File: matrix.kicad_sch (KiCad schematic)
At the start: 154 parts

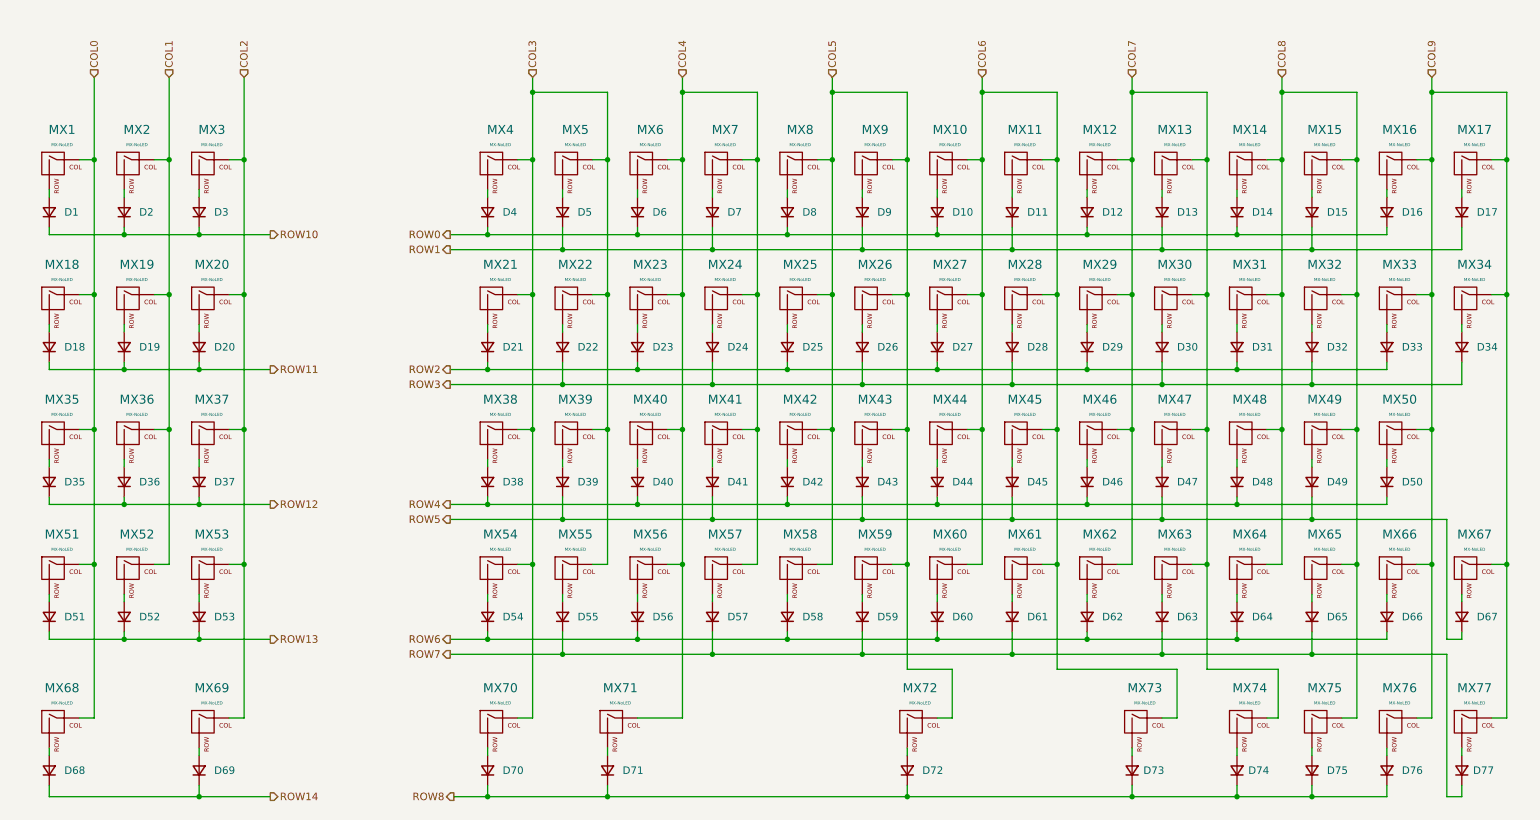
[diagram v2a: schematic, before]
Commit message: Assigned footprints, key labels and placed key switches on PCB. Removed SWD component.
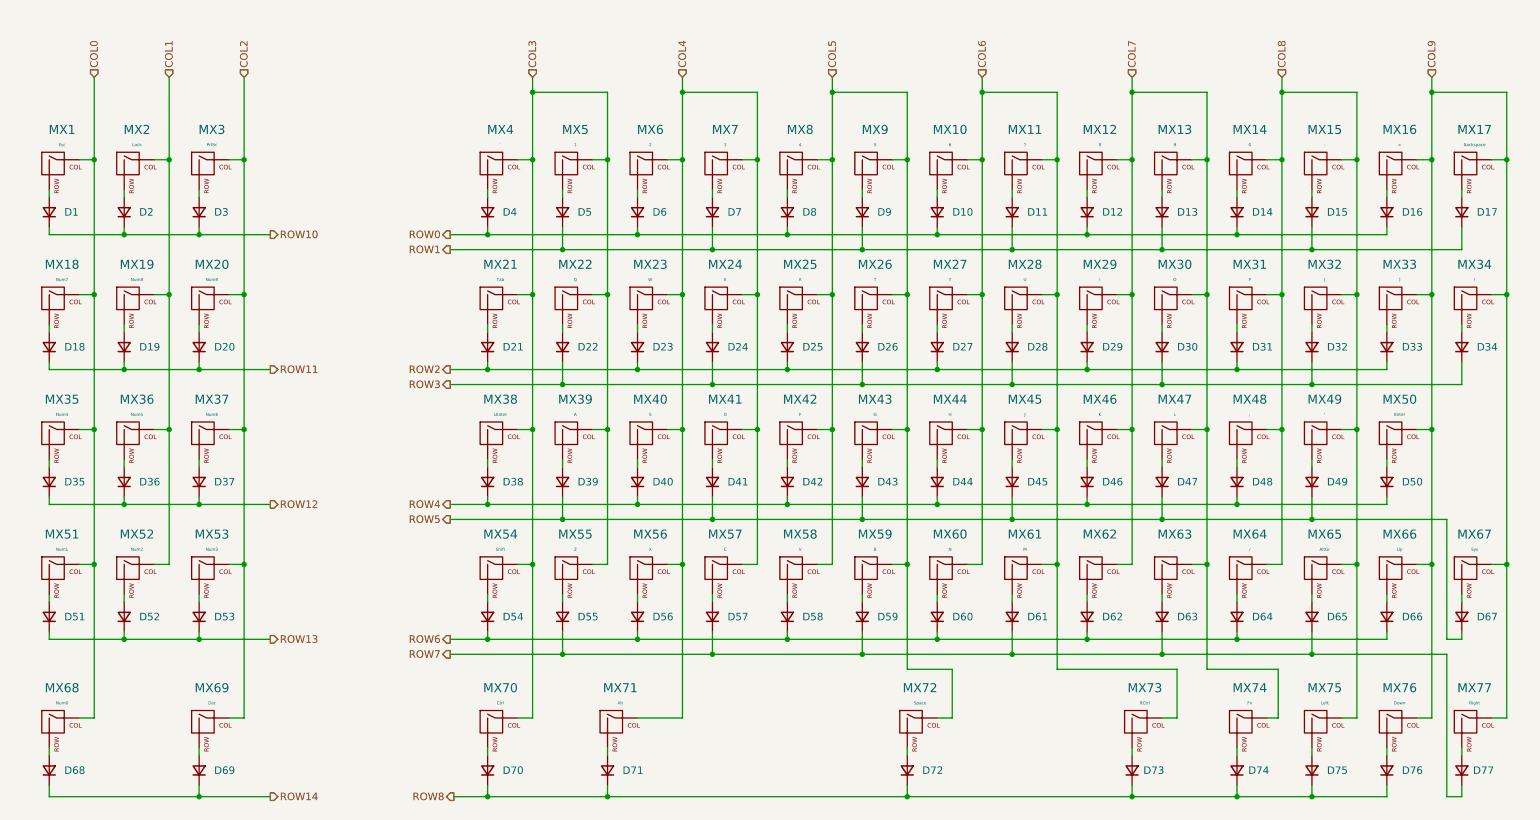
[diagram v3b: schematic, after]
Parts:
- D1, D10, D11, D12, D13, D14, D15, D16, D17, D18, D19, D2, D20, D21, D22, D23, D24, D25, D26, D27, D28, D29, D3, D30, D31, D32, D33, D34, D35, D36, D37, D38, D39, D4, D40, D41, D42, D43, D44, D45, D46, D47, D48, D49, D5, D50, D51, D52, D53, D54, D55, D56, D57, D58, D59, D6, D60, D61, D62, D63, D64, D65, D66, D67, D68, D69, D7, D70, D71, D72, D73, D74, D75, D76, D77, D8, D9: footprint (none) -> Diode_SMD:D_SOD-123
- MX1: value MX-NoLED -> Esc; footprint (none) -> MX_Only:MXOnly-1U-NoLED
- MX10: value MX-NoLED -> 6; footprint (none) -> MX_Only:MXOnly-1U-NoLED
- MX11: value MX-NoLED -> 7; footprint (none) -> MX_Only:MXOnly-1U-NoLED
- MX12: value MX-NoLED -> 8; footprint (none) -> MX_Only:MXOnly-1U-NoLED
- MX13: value MX-NoLED -> 9; footprint (none) -> MX_Only:MXOnly-1U-NoLED
- MX14: value MX-NoLED -> 0; footprint (none) -> MX_Only:MXOnly-1U-NoLED
- MX15: value MX-NoLED -> -; footprint (none) -> MX_Only:MXOnly-1U-NoLED
- MX16: value MX-NoLED -> =; footprint (none) -> MX_Only:MXOnly-1U-NoLED
- MX17: value MX-NoLED -> Backspace; footprint (none) -> MX_Only:MXOnly-2U-NoLED
- MX18: value MX-NoLED -> Num7; footprint (none) -> MX_Only:MXOnly-1U-NoLED
- MX19: value MX-NoLED -> Num8; footprint (none) -> MX_Only:MXOnly-1U-NoLED
- MX2: value MX-NoLED -> Lock; footprint (none) -> MX_Only:MXOnly-1U-NoLED
- MX20: value MX-NoLED -> Num9; footprint (none) -> MX_Only:MXOnly-1U-NoLED
- MX21: value MX-NoLED -> Tab; footprint (none) -> MX_Only:MXOnly-1.5U-NoLED
- MX22: value MX-NoLED -> Q; footprint (none) -> MX_Only:MXOnly-1U-NoLED
- MX23: value MX-NoLED -> W; footprint (none) -> MX_Only:MXOnly-1U-NoLED
- MX24: value MX-NoLED -> E; footprint (none) -> MX_Only:MXOnly-1U-NoLED
- MX25: value MX-NoLED -> R; footprint (none) -> MX_Only:MXOnly-1U-NoLED
- MX26: value MX-NoLED -> T; footprint (none) -> MX_Only:MXOnly-1U-NoLED
- MX27: value MX-NoLED -> Y; footprint (none) -> MX_Only:MXOnly-1U-NoLED
- MX28: value MX-NoLED -> U; footprint (none) -> MX_Only:MXOnly-1U-NoLED
- MX29: value MX-NoLED -> I; footprint (none) -> MX_Only:MXOnly-1U-NoLED
- MX3: value MX-NoLED -> PrtSc; footprint (none) -> MX_Only:MXOnly-1U-NoLED
- MX30: value MX-NoLED -> O; footprint (none) -> MX_Only:MXOnly-1U-NoLED
- MX31: value MX-NoLED -> P; footprint (none) -> MX_Only:MXOnly-1U-NoLED
- MX32: value MX-NoLED -> [; footprint (none) -> MX_Only:MXOnly-1U-NoLED
- MX33: value MX-NoLED -> ]; footprint (none) -> MX_Only:MXOnly-1U-NoLED
- MX34: value MX-NoLED -> \; footprint (none) -> MX_Only:MXOnly-1.5U-NoLED
- MX35: value MX-NoLED -> Num4; footprint (none) -> MX_Only:MXOnly-1U-NoLED
- MX36: value MX-NoLED -> Num5; footprint (none) -> MX_Only:MXOnly-1U-NoLED
- MX37: value MX-NoLED -> Num6; footprint (none) -> MX_Only:MXOnly-1U-NoLED
- MX38: value MX-NoLED -> LEnter; footprint (none) -> MX_Only:MXOnly-1.75U-NoLED
- MX39: value MX-NoLED -> A; footprint (none) -> MX_Only:MXOnly-1U-NoLED
- MX4: value MX-NoLED -> `; footprint (none) -> MX_Only:MXOnly-1U-NoLED
- MX40: value MX-NoLED -> S; footprint (none) -> MX_Only:MXOnly-1U-NoLED
- MX41: value MX-NoLED -> D; footprint (none) -> MX_Only:MXOnly-1U-NoLED
- MX42: value MX-NoLED -> F; footprint (none) -> MX_Only:MXOnly-1U-NoLED
- MX43: value MX-NoLED -> G; footprint (none) -> MX_Only:MXOnly-1U-NoLED
- MX44: value MX-NoLED -> H; footprint (none) -> MX_Only:MXOnly-1U-NoLED
- MX45: value MX-NoLED -> J; footprint (none) -> MX_Only:MXOnly-1U-NoLED
- MX46: value MX-NoLED -> K; footprint (none) -> MX_Only:MXOnly-1U-NoLED
- MX47: value MX-NoLED -> L; footprint (none) -> MX_Only:MXOnly-1U-NoLED
- MX48: value MX-NoLED -> ;; footprint (none) -> MX_Only:MXOnly-1U-NoLED
- MX49: value MX-NoLED -> '; footprint (none) -> MX_Only:MXOnly-1U-NoLED
- MX5: value MX-NoLED -> 1; footprint (none) -> MX_Only:MXOnly-1U-NoLED
- MX50: value MX-NoLED -> Enter; footprint (none) -> MX_Only:MXOnly-2.25U-NoLED
- MX51: value MX-NoLED -> Num1; footprint (none) -> MX_Only:MXOnly-1U-NoLED
- MX52: value MX-NoLED -> Num2; footprint (none) -> MX_Only:MXOnly-1U-NoLED
- MX53: value MX-NoLED -> Num3; footprint (none) -> MX_Only:MXOnly-1U-NoLED
- MX54: value MX-NoLED -> Shift; footprint (none) -> MX_Only:MXOnly-2U-NoLED
- MX55: value MX-NoLED -> Z; footprint (none) -> MX_Only:MXOnly-1U-NoLED
- MX56: value MX-NoLED -> X; footprint (none) -> MX_Only:MXOnly-1U-NoLED
- MX57: value MX-NoLED -> C; footprint (none) -> MX_Only:MXOnly-1U-NoLED
- MX58: value MX-NoLED -> V; footprint (none) -> MX_Only:MXOnly-1U-NoLED
- MX59: value MX-NoLED -> B; footprint (none) -> MX_Only:MXOnly-1U-NoLED
- MX6: value MX-NoLED -> 2; footprint (none) -> MX_Only:MXOnly-1U-NoLED
- MX60: value MX-NoLED -> N; footprint (none) -> MX_Only:MXOnly-1U-NoLED
- MX61: value MX-NoLED -> M; footprint (none) -> MX_Only:MXOnly-1U-NoLED
- MX62: value MX-NoLED -> ,; footprint (none) -> MX_Only:MXOnly-1U-NoLED
- MX63: value MX-NoLED -> .; footprint (none) -> MX_Only:MXOnly-1U-NoLED
- MX64: value MX-NoLED -> /; footprint (none) -> MX_Only:MXOnly-1U-NoLED
- MX65: value MX-NoLED -> AltGr; footprint (none) -> MX_Only:MXOnly-1U-NoLED
- MX66: value MX-NoLED -> Up; footprint (none) -> MX_Only:MXOnly-1U-NoLED
- MX67: value MX-NoLED -> Sys; footprint (none) -> MX_Only:MXOnly-1U-NoLED
- MX68: value MX-NoLED -> Num0; footprint (none) -> MX_Only:MXOnly-2U-NoLED
- MX69: value MX-NoLED -> Dot; footprint (none) -> MX_Only:MXOnly-1U-NoLED
- MX7: value MX-NoLED -> 3; footprint (none) -> MX_Only:MXOnly-1U-NoLED
- MX70: value MX-NoLED -> Ctrl; footprint (none) -> MX_Only:MXOnly-1.25U-NoLED
- MX71: value MX-NoLED -> Alt; footprint (none) -> MX_Only:MXOnly-1.25U-NoLED
- MX72: value MX-NoLED -> Space; footprint (none) -> MX_Only:MXOnly-7U-NoLED
- MX73: value MX-NoLED -> RCtrl; footprint (none) -> MX_Only:MXOnly-1.25U-NoLED
- MX74: value MX-NoLED -> Fn; footprint (none) -> MX_Only:MXOnly-1.25U-NoLED
- MX75: value MX-NoLED -> Left; footprint (none) -> MX_Only:MXOnly-1U-NoLED
- MX76: value MX-NoLED -> Down; footprint (none) -> MX_Only:MXOnly-1U-NoLED
- MX77: value MX-NoLED -> Right; footprint (none) -> MX_Only:MXOnly-1U-NoLED
- MX8: value MX-NoLED -> 4; footprint (none) -> MX_Only:MXOnly-1U-NoLED
- MX9: value MX-NoLED -> 5; footprint (none) -> MX_Only:MXOnly-1U-NoLED

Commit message: Shuffled MCU pins and realigned schema to 50 mils, but USB connector is not connected.
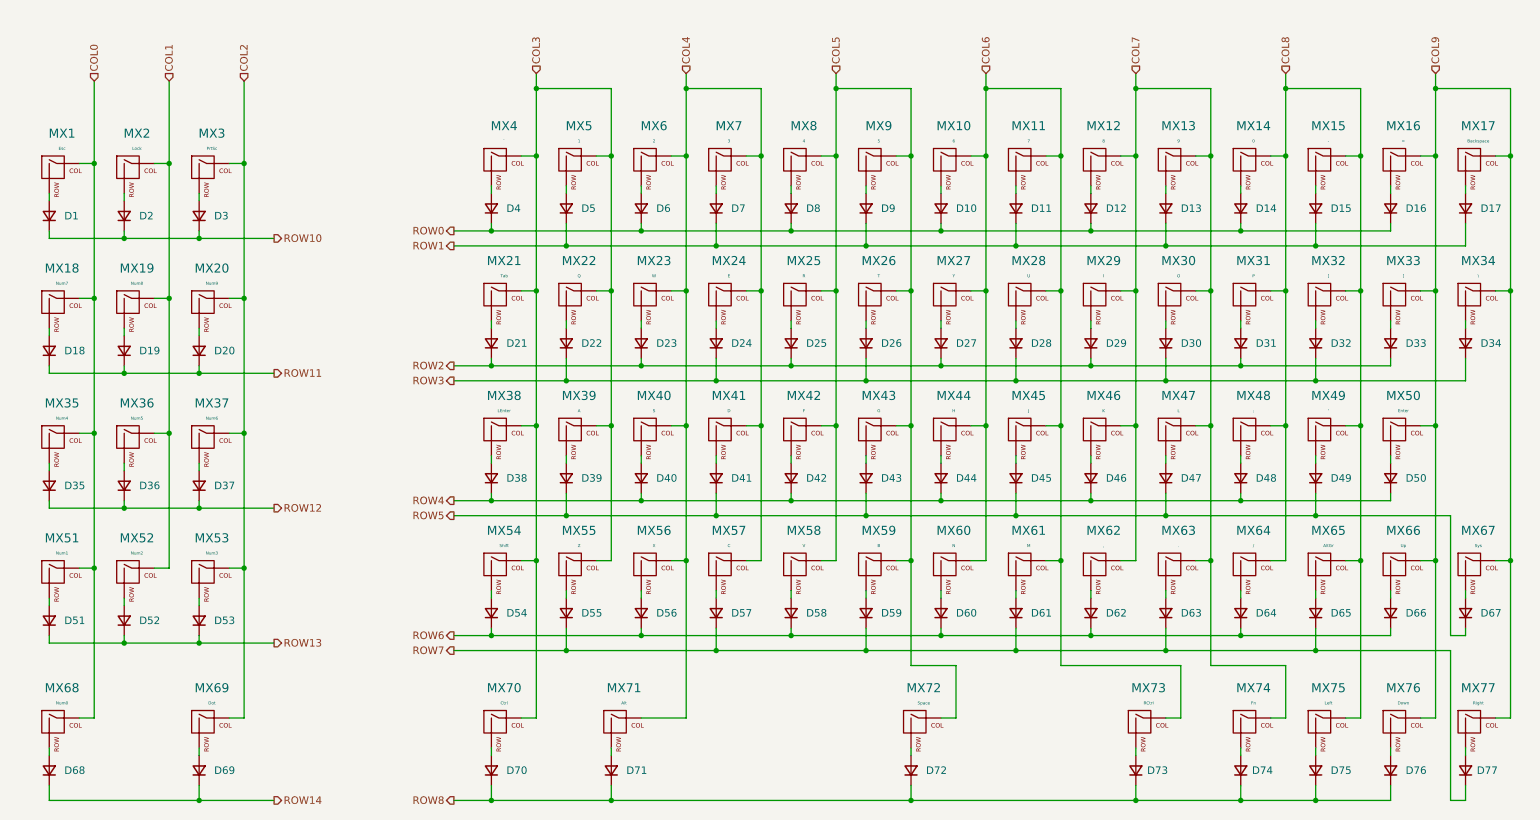
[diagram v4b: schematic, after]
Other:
- moved on the sheet: D1, D10, D11, D12, D13, D14, D15, D16, D17, D18, D19, D2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

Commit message: Routing the matrices, but I might redo the pin assignments again.
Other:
- title: (none) -> Intfield77
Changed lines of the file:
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@@
 (kicad_sch (version 20230121) (generator eeschema)
   (paper "A4")
+  (title_block
+    (title "Intfield77")
+    (date "2023-08-20")
+    (rev "0.1")
+  )
   (junction (at 214.63 78.74) (diameter 0) (color 0 0 0 0)
   )

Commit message: Changed the silkscreen for the MX footprints.
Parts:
- MX1, MX10, MX11, MX12, MX13, MX14, MX15, MX16, MX18, MX19, MX2, MX20, MX22, MX23, MX24, MX25, MX26, MX27, MX28, MX29, MX3, MX30, MX31, MX32, MX33, MX35, MX36, MX37, MX39, MX4, MX40, MX41, MX42, MX43, MX44, MX45, MX46, MX47, MX48, MX49, MX5, MX51, MX52, MX53, MX55, MX56, MX57, MX58, MX59, MX6, MX60, MX61, MX62, MX63, MX64, MX65, MX66, MX67, MX69, MX7, MX75, MX76, MX77, MX8, MX9: footprint MX_Only:MXOnly-1U-NoLED -> local:MXOnly-1U-NoLED
- MX17, MX54, MX68: footprint MX_Only:MXOnly-2U-NoLED -> local:MXOnly-2U-NoLED
- MX21, MX34: footprint MX_Only:MXOnly-1.5U-NoLED -> local:MXOnly-1.5U-NoLED
- MX38: footprint MX_Only:MXOnly-1.75U-NoLED -> local:MXOnly-1.75U-NoLED
- MX50: footprint MX_Only:MXOnly-2.25U-NoLED -> local:MXOnly-2.25U-NoLED
- MX70, MX71, MX73, MX74: footprint MX_Only:MXOnly-1.25U-NoLED -> local:MXOnly-1.25U-NoLED
- MX72: footprint MX_Only:MXOnly-7U-NoLED -> local:MXOnly-7U-NoLED
